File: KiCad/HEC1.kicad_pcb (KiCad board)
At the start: 2 copper layers, 243.8 x 170.2 mm, 639 parts, among them J1 Barrel_Jack_Switch, J2 Conn_02x12_Odd_Even, J3 Conn_02x05_Odd_Even, J5 Screw_Terminal_01x02, J6 DE9_Plug_MountingHoles, J7 AudioJack3, J8 NES_Port_Male, J9 Conn_02x14_Odd_Even, SW1 SW_DIP_x04, SW2 SW_Push, U1 Z80CPU, U10 74LS32, U11 74LS00, U12 74LS04, U13 74LS245, U14 74LS245, U15 74LS32, U16 74LS32, U17 74LS20, U18 74LS138, U19 74LS30, U2 AS6C4008-55PCN, U20 74LS574, U21 74LS574, U22 74LS02, U23 74LS74, U24 74LS74, U25 74LS541, U26 74LS541, U27 74LS74, U28 74LS30, U29 74LS74, U3 AS6C4008-55PCN, U30 74LS74, U31 74LS32, U32 LM79M05_TO220, U33 74LS20, U34 74LS393, U35 74LS08, U36 74LS574, U37 74LS32, U38 74LS47, U39 74LS47, U4 CY7C199, U40 DA04-11EWA, U41 74LS02, U42 74LS06, U44 74LS541, U5 CY7C199, U6 74LS138, U7 28C256, U8 74LS138, U9 74LS574, X1 CXO_DIP8, Y1 Crystal

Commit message: End of livestream
State of the project at the end of the livestream, still not finished.
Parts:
- removed the REF** at (185.4, 63.5)
- removed the REF** at (160.0, 76.2)
- removed the REF** at (170.2, 76.2)
- removed the REF** at (182.9, 76.2)
- removed the REF** at (162.6, 76.2)
- removed the REF** at (185.4, 73.7)
- removed the REF** at (177.8, 76.2)
- removed the REF** at (185.4, 76.2)
- removed the REF** at (185.4, 68.6)
- removed the REF** at (165.1, 76.2)
- removed the REF** at (172.7, 76.2)
- removed the REF** at (167.6, 76.2)
- removed the REF** at (185.4, 58.4)
- removed the REF** at (175.3, 76.2)
- removed the REF** at (180.3, 76.2)
- removed the REF** at (185.4, 61.0)
- removed the REF** at (185.4, 55.9)
- removed the REF** at (185.4, 66.0)
- removed the REF** at (185.4, 50.8)
- removed the REF** at (185.4, 71.1)
- removed the REF** at (185.4, 53.3)
- moved RN1 1.27 mm to (125.7, 132.1)
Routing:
- net /HEC_Protection/~{VDP_IRQ}: track 23.5 -> 211.2 mm, vias 0 -> 2
- net /HEC_IO/~{IO_CS2}: track 25.9 -> 213.1 mm, vias 0 -> 4
- net /HEC_IO/~{IO_CS3}: track 14.5 -> 200.6 mm, vias 0 -> 4
- net /HEC_Peripherals/~{MS_IRQ}: track 47.5 -> 208.3 mm
- net /HEC_Peripherals/~{KB_IRQ}: track 43.7 -> 200.0 mm, vias 0 -> 1
- net Net-(U11-Pad2): track 0.00 -> 78.2 mm, vias 0 -> 2
- net /HEC_CPU/~{RESET}: track 179.2 -> 252.4 mm, vias 1 -> 2
- net /HEC_CPU/~{IORQ}: track 20.5 -> 90.1 mm, vias 0 -> 2
- net /HEC_IO/D4: track 450.0 -> 510.2 mm, vias 8 -> 11
- net /HEC_Protection/~{XFAULT}: track 65.2 -> 122.1 mm, vias 2 -> 4
- net /HEC_Memory/~{PID}: track 0.00 -> 53.9 mm
- net /HEC_CPU/~{RAMEN}: track 0.00 -> 50.1 mm
- net /HEC_Protection/~{CLRINT}: track 59.0 -> 108.1 mm
- net /HEC_IO/D7: track 493.6 -> 542.1 mm, vias 7 -> 9
- net /HEC_IO/~{IRQ3}: track 15.9 -> 62.3 mm, vias 0 -> 1
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
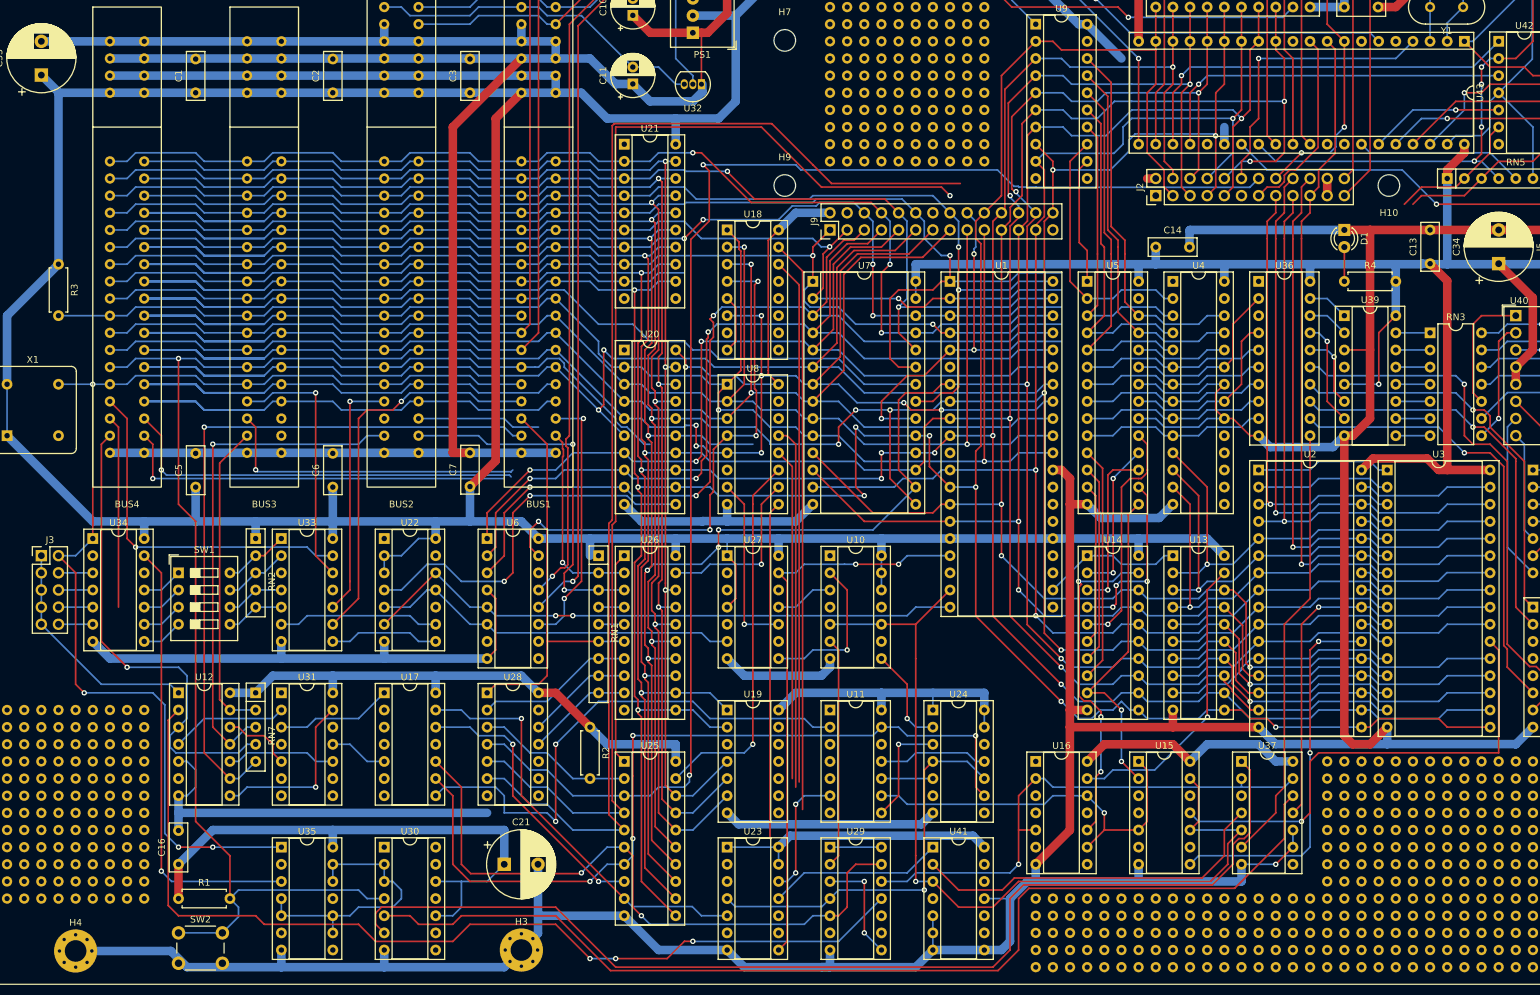
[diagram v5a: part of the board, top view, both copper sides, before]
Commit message: Bottom left routing complete
Finished routing the bottom left side of the PCB (wait generation and part of protection). Minor changes to schematic to ease routing.
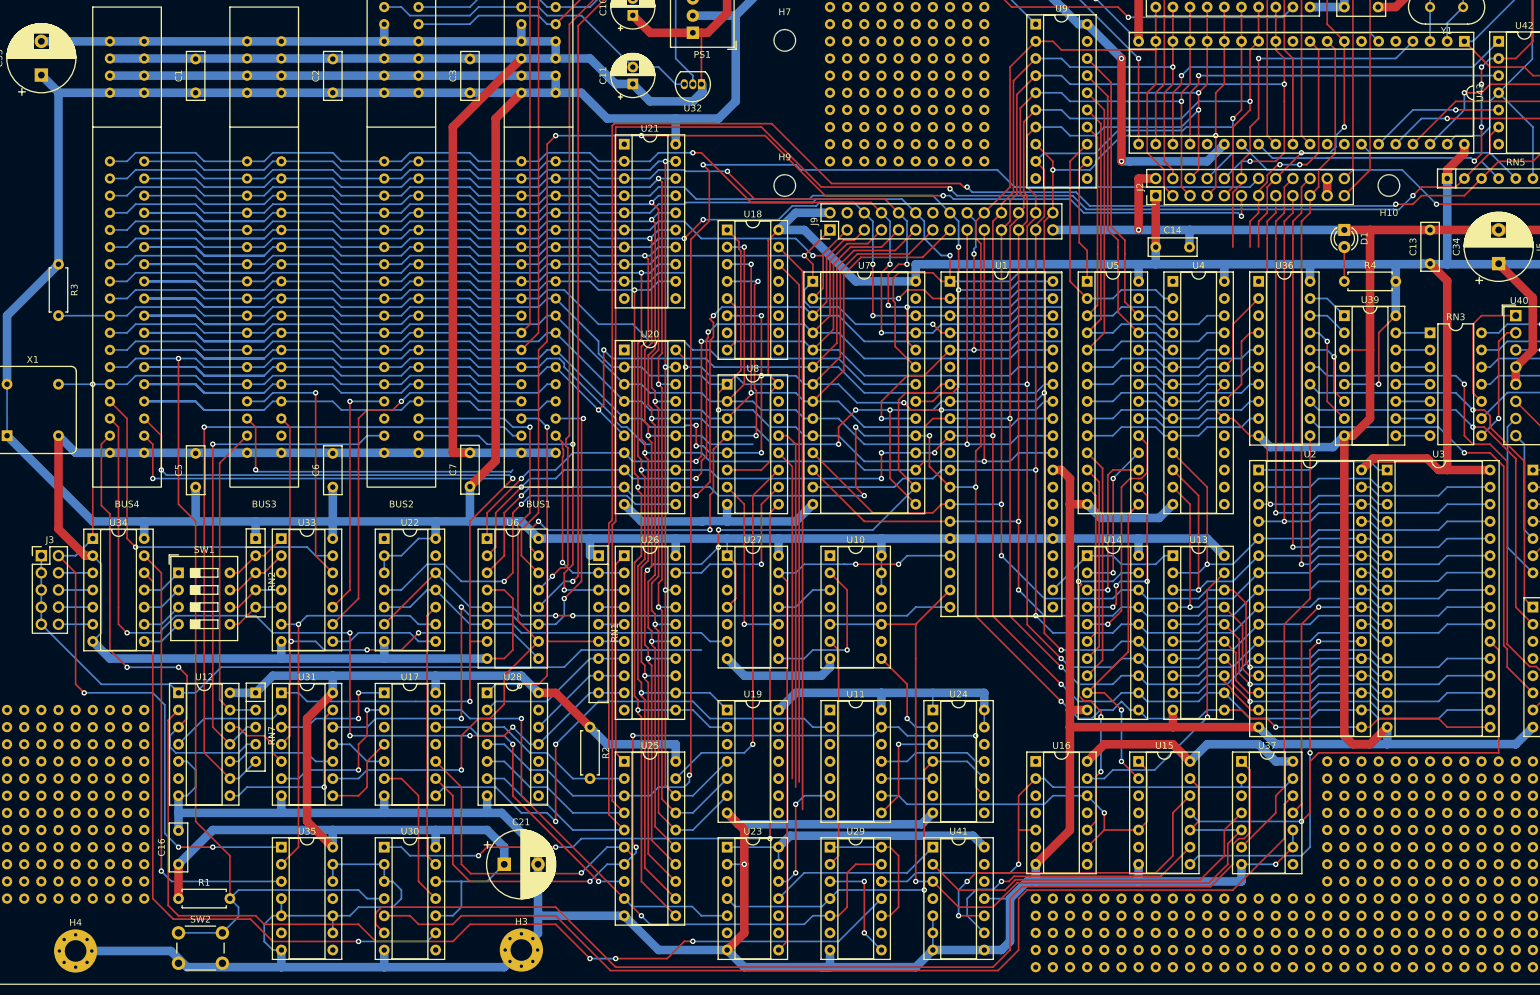
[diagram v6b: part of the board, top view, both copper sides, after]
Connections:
- U4 pad 25: /HEC_Memory/PROC_ID5 -> /HEC_Memory/PROC_ID0
- U4 pad 3: /HEC_Memory/PROC_ID1 -> /HEC_Memory/PROC_ID4
- U4 pad 4: /HEC_Memory/PROC_ID0 -> /HEC_Memory/PROC_ID1
- U4 pad 5: /HEC_Memory/PROC_ID4 -> /HEC_Memory/PROC_ID5
- U5 pad 25: /HEC_Memory/PROC_ID5 -> /HEC_Memory/PROC_ID0
- U5 pad 3: /HEC_Memory/PROC_ID1 -> /HEC_Memory/PROC_ID4
- U5 pad 4: /HEC_Memory/PROC_ID0 -> /HEC_Memory/PROC_ID1
- U5 pad 5: /HEC_Memory/PROC_ID4 -> /HEC_Memory/PROC_ID5
- U9 pad 14: /HEC_Memory/PROC_ID1 -> /HEC_Memory/PROC_ID4
- U9 pad 15: /HEC_Memory/PROC_ID0 -> /HEC_Memory/PROC_ID1
- U9 pad 16: /HEC_Memory/PROC_ID4 -> /HEC_Memory/PROC_ID5
- U9 pad 17: /HEC_Memory/PROC_ID5 -> /HEC_Memory/PROC_ID0
- U9 pad 4: /HEC_IO/D5 -> /HEC_IO/D0
- U9 pad 5: /HEC_IO/D4 -> /HEC_IO/D5
- U9 pad 6: /HEC_IO/D0 -> /HEC_IO/D1
- U9 pad 7: /HEC_IO/D1 -> /HEC_IO/D4
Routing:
- net /HEC_IO/~{IO_CS1}: track 0.00 -> 177.5 mm, vias 0 -> 4
- net L: track 1513.4 -> 1643.9 mm, vias 1 -> 3
- net H: track 1418.0 -> 1535.2 mm, vias 2 -> 4
- net Net-(U30B-Q): track 0.00 -> 93.9 mm, vias 0 -> 1
- net /HEC_IO/~{IO_CS6}: track 0.00 -> 89.3 mm, vias 0 -> 3
- net /HEC_IO/~{IRQ4}: track 44.3 -> 128.8 mm, vias 0 -> 5
- net /HEC_CPU/CLK: track 34.7 -> 114.8 mm
- net /HEC_IO/~{IO_CS5}: track 18.3 -> 95.1 mm, vias 0 -> 2
- net /HEC_IO/~{IO_CS7}: track 60.9 -> 130.5 mm, vias 1 -> 3
- net /HEC_Peripherals/~{MS_IRQ}: track 208.3 -> 276.9 mm, vias 0 -> 2
- net /HEC_Peripherals/~{KB_IRQ}: track 200.0 -> 268.4 mm, vias 1 -> 2
- net /HEC_CPU/~{RAMEN}: track 50.1 -> 108.8 mm, vias 0 -> 3
- net /HEC_Memory/~{RAM_A19}: track 0.00 -> 51.4 mm, vias 0 -> 2
- net /HEC_IO/~{IO_CS4}: track 38.8 -> 87.4 mm, vias 2 -> 4
- net /HEC_Memory/RAM_A19: track 34.9 -> 77.2 mm, vias 1 -> 2
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
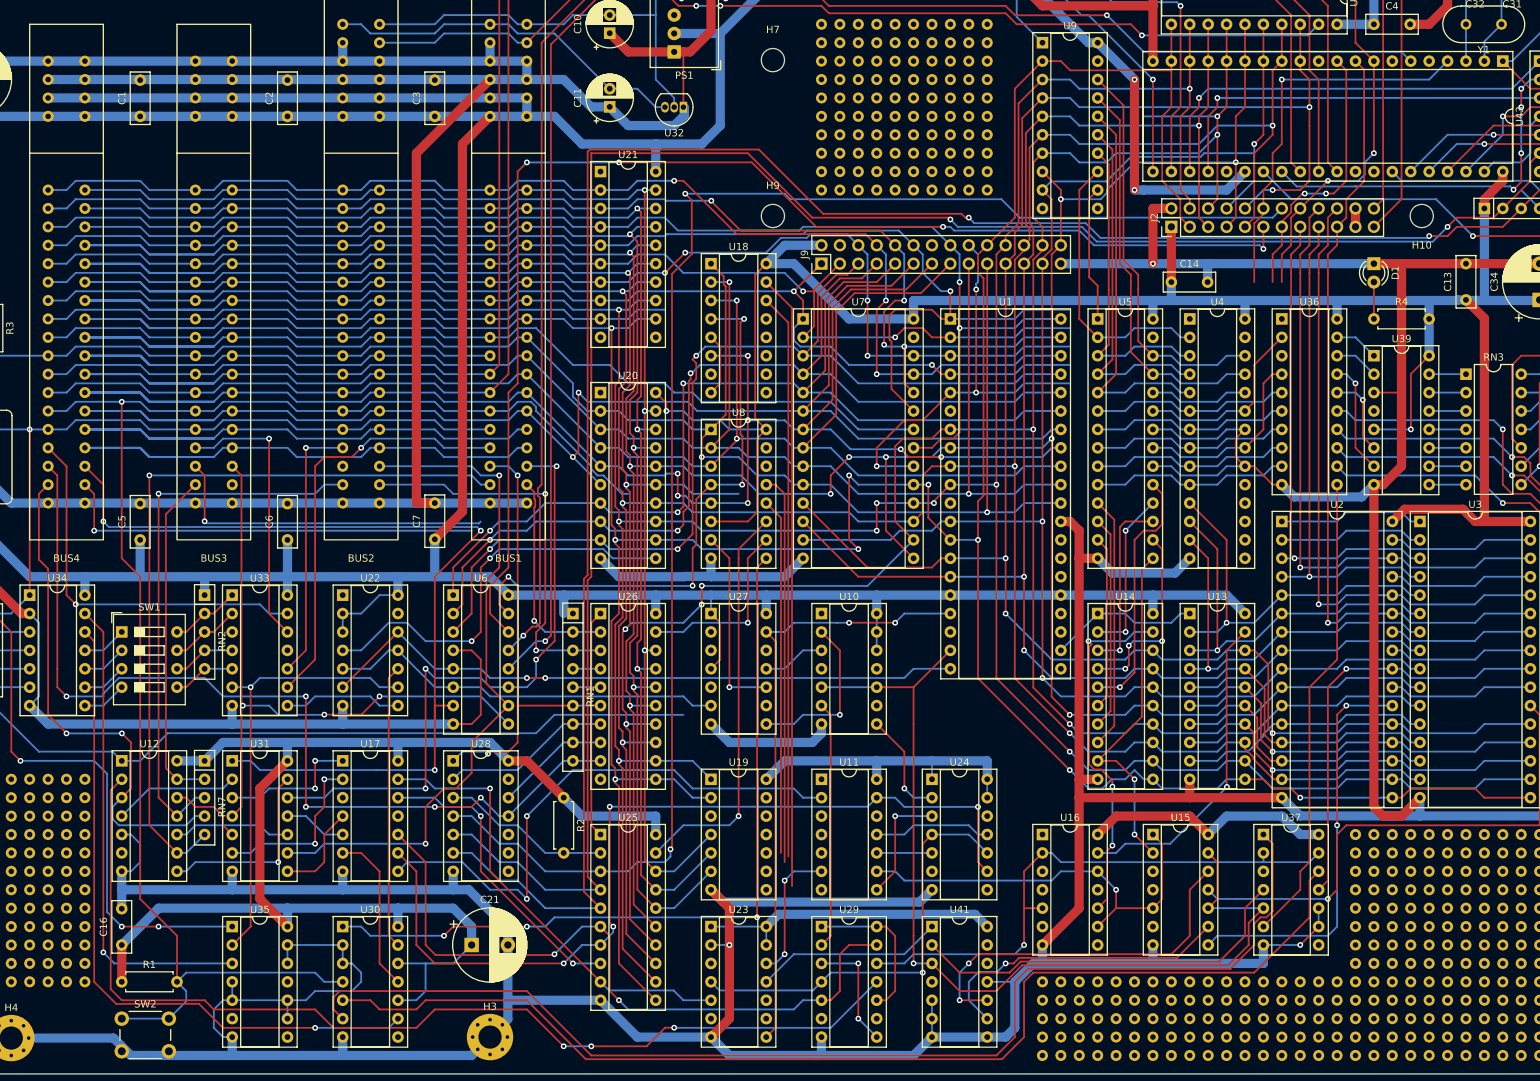
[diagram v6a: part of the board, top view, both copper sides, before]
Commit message: More routing
Routing starts to become harder since most of the board is occupied. I should REALLY use a set of constraints that allow me to route two traces between adjacent pads...
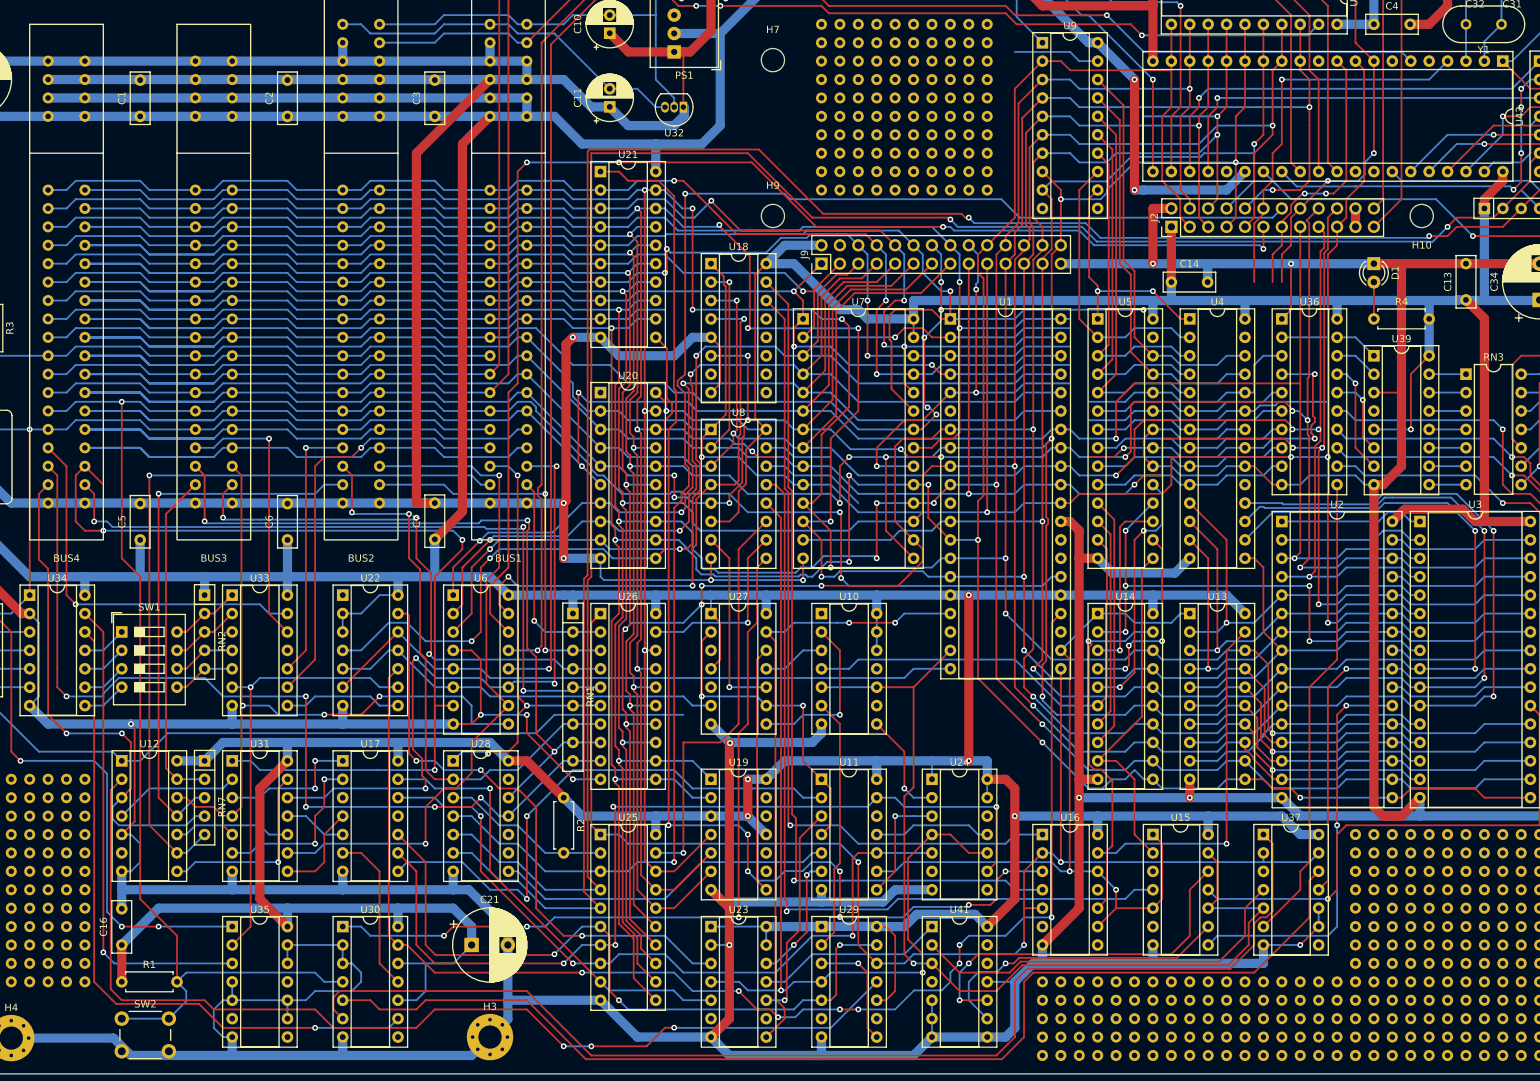
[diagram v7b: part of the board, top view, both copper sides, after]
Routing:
- net Net-(U21-OE): track 0.00 -> 168.7 mm, vias 0 -> 7
- net /HEC_CPU/~{WAIT}: track 39.2 -> 183.8 mm, vias 0 -> 8
- net L: track 1643.9 -> 1780.5 mm, vias 3 -> 16
- net /HEC_IO/D1: track 430.0 -> 525.0 mm, vias 6 -> 12
- net Net-(U23A-C): track 0.00 -> 82.5 mm, vias 0 -> 3
- net /HEC_CPU/~{RD}: track 162.6 -> 241.5 mm, vias 3 -> 5
- net H: track 1535.2 -> 1613.7 mm, vias 4 -> 9
- net /HEC_IO/D0: track 453.8 -> 527.1 mm, vias 8 -> 12
- net /HEC_IO/~{SENSE3}: track 3.81 -> 76.2 mm, vias 0 -> 3
- net /HEC_CPU/~{RESET}: track 263.1 -> 334.1 mm, vias 2 -> 4
- net /HEC_Memory/RAM_A14: track 34.9 -> 105.5 mm, vias 0 -> 2
- net /HEC_Memory/RAM_A13: track 34.9 -> 101.1 mm, vias 0 -> 2
- net /HEC_Memory/RAM_A12: track 34.9 -> 97.0 mm, vias 0 -> 2
- net /HEC_Memory/~{PID}: track 53.9 -> 112.5 mm, vias 0 -> 1
- net /HEC_IO/~{IRQ2}: track 23.5 -> 78.9 mm, vias 0 -> 2
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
